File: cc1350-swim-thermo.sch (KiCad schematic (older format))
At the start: 54 parts, among them P1 LMT_70_1, P2 LMT_70_2, P3 SMA FEMALE, P4 USB_OTG, P5 CONN_02X05, Q1 2N7002, SW1 SW_Push, U1 2450BM14G0011T, U2 XMSSJE3G0PA-003, U3 CC1350F128RSM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

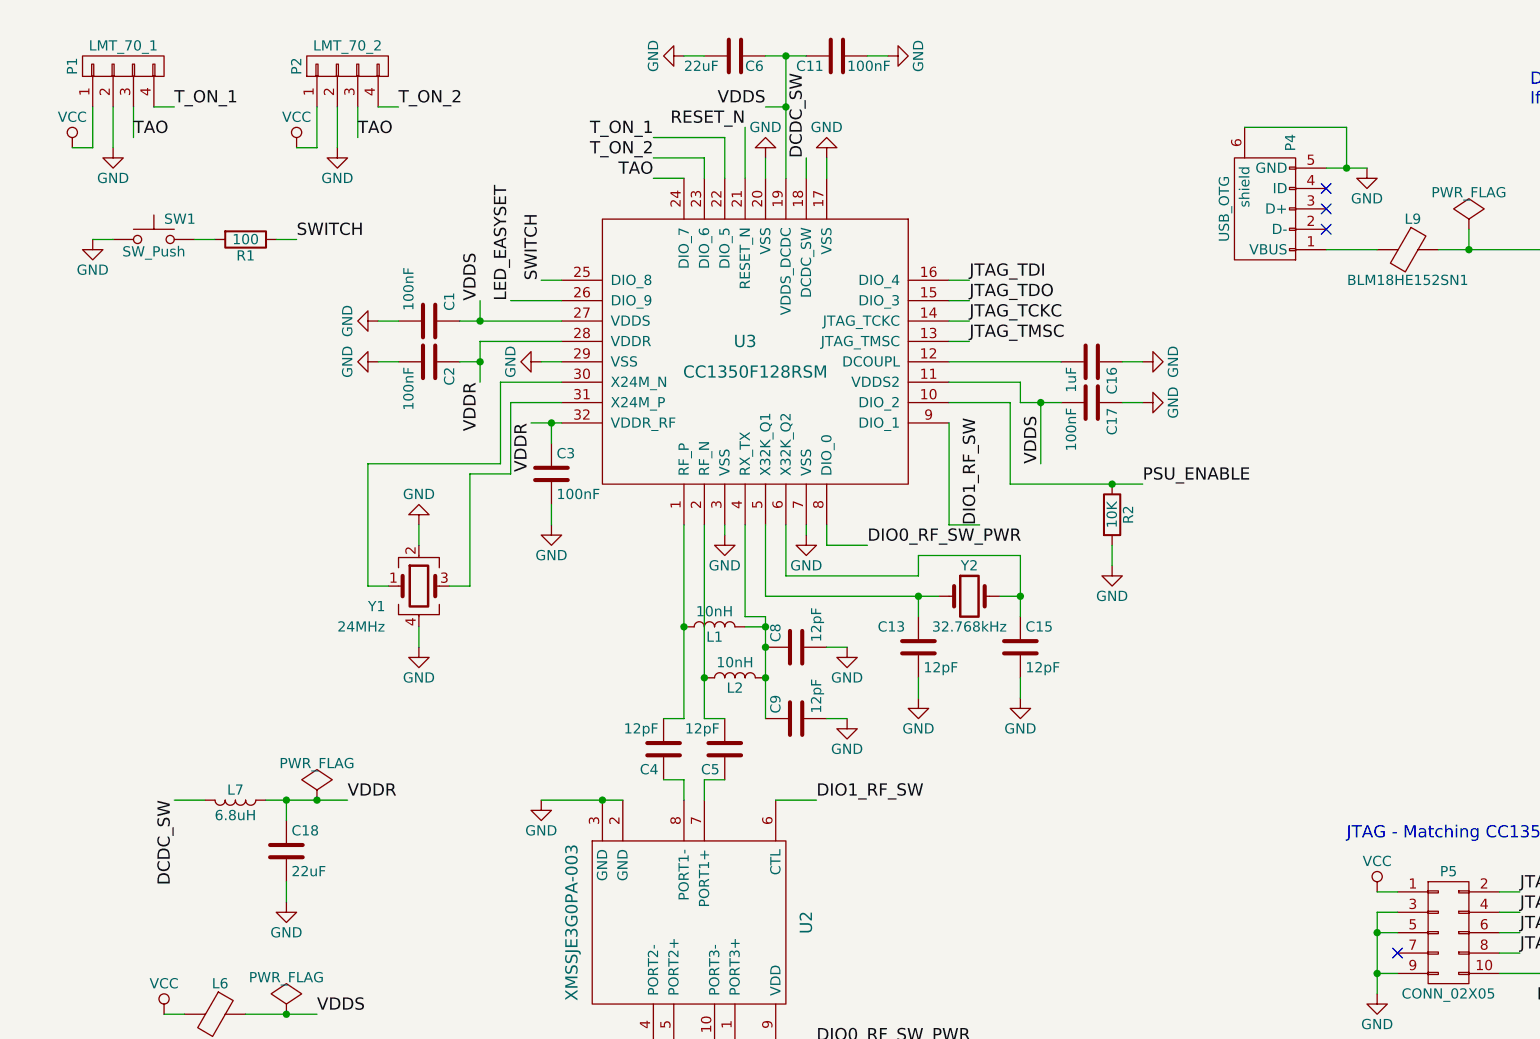
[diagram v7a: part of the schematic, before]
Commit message: wired all components
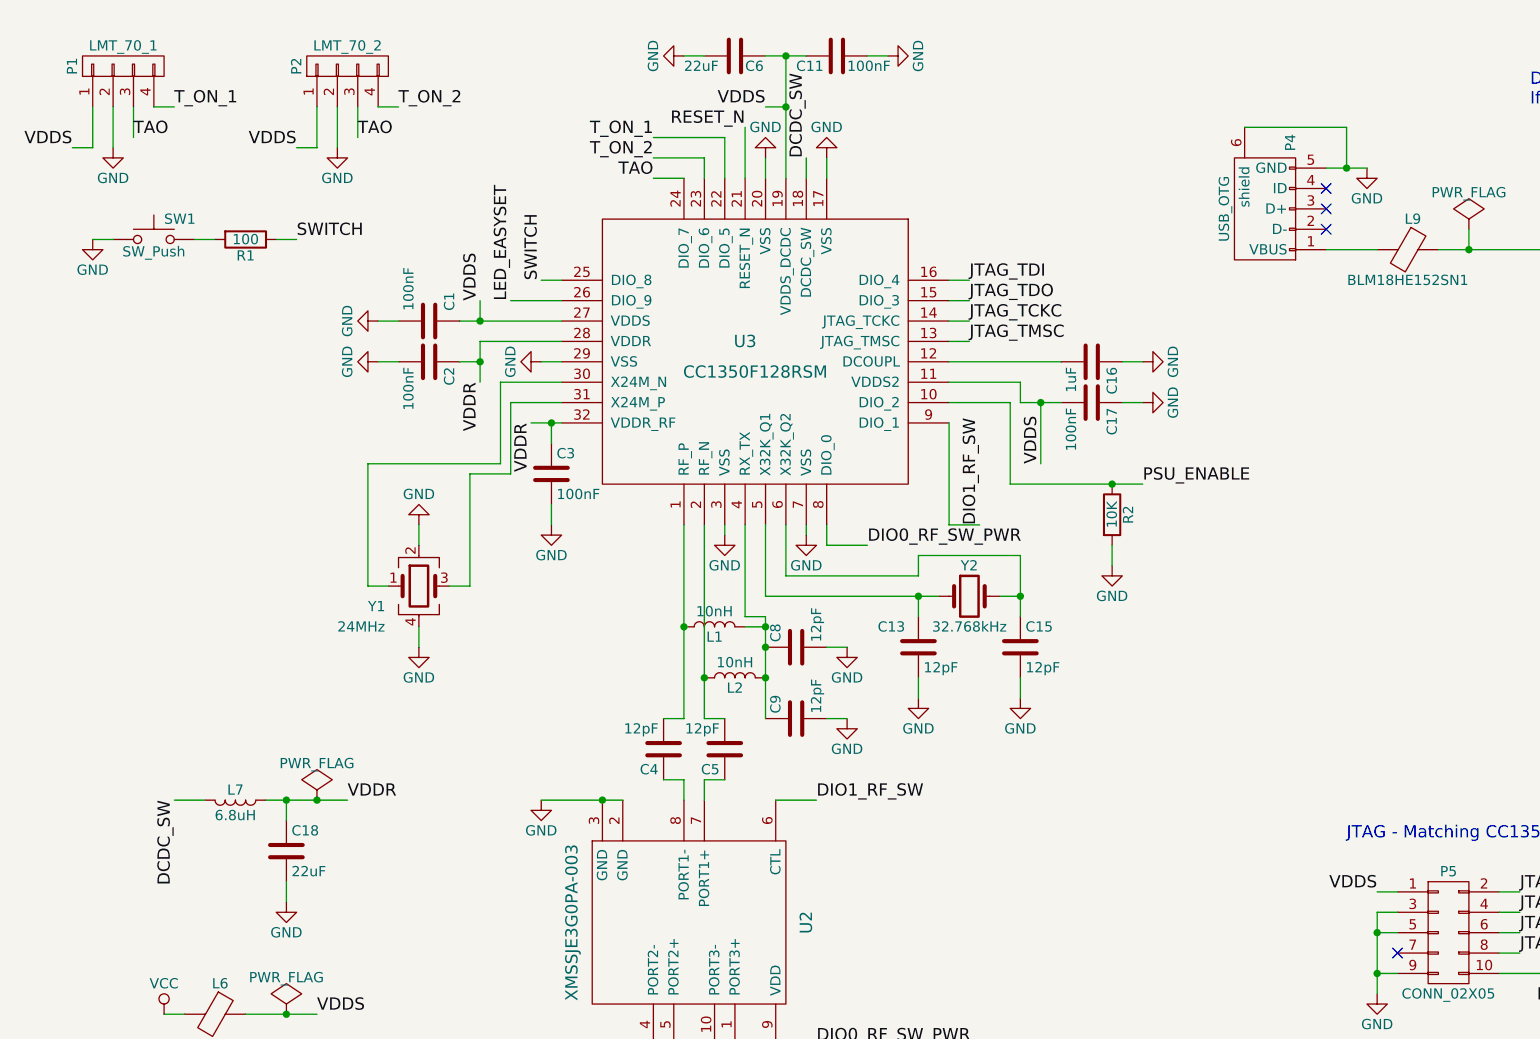
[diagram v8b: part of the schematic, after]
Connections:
- net VCC: no longer P1.1 (P1), P2.1 (P1), P5.1 (P1)
- net VDDS: now also P1.1 (P1), P2.1 (P1), P5.1 (P1)
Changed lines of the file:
@@
 	0    1    1    0
 $EndComp
-Text Label 2050 5550 0    60   ~ 0
-VDDS
 Text Label 1350 4500 3    60   ~ 0
 DCDC_SW
@@
 	1    0    0    -1
 $EndComp
-$Comp
-L VCC #PWR045
-U 1 1 58CA0128
-P 7250 4950
-F 0 "#PWR045" H 7250 4800 50  0001 C CNN
-F 1 "VCC" H 7250 5100 50  0000 C CNN
-F 2 "" H 7250 4950 50  0000 C CNN
-F 3 "" H 7250 4950 50  0000 C CNN
-	1    7250 4950
-	1    0    0    -1
-$EndComp
 NoConn ~ 7350 5250
 $Comp
@@
 	1    0    0    -1
 $EndComp
-$Comp
-L VCC #PWR050
-U 1 1 58CC7CED
-P 850 1300
-F 0 "#PWR050" H 850 1150 50  0001 C CNN
-F 1 "VCC" H 850 1450 50  0000 C CNN
-F 2 "" H 850 1300 50  0000 C CNN
-F 3 "" H 850 1300 50  0000 C CNN
-	1    850  1300
-	1    0    0    -1
-$EndComp
 Text Label 1150 1250 0    60   ~ 0
 TAO
@@
 F 3 "" H 2150 1300 50  0000 C CNN
 	1    2150 1300
-	1    0    0    -1
-$EndComp
-$Comp
-L VCC #PWR052
-U 1 1 58CC91CD
-P 1950 1300
-F 0 "#PWR052" H 1950 1150 50  0001 C CNN
-F 1 "VCC" H 1950 1450 50  0000 C CNN
-F 2 "" H 1950 1300 50  0000 C CNN
-F 3 "" H 1950 1300 50  0000 C CNN
-	1    1950 1300
 	1    0    0    -1
 $EndComp
@@
 Wire Wire Line
 	3350 7400 3350 7550
+Text Label 2050 5550 0    60   ~ 0
+VDDS
+Text Label 7250 4950 2    60   ~ 0
+VDDS
+Text Label 850  1300 2    60   ~ 0
+VDDS
+Text Label 1950 1300 2    60   ~ 0
+VDDS
 $EndSCHEMATC
